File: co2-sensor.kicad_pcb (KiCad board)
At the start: 2 copper layers, 159.5 x 116 mm, 20 parts, among them J1 E-Ink Display, Q1 Si1308EDL

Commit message: Rework to use ESP32 module directly
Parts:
- removed A2: Adafruit Feather, Module:Adafruit_Feather
- added C11: 10uF, Capacitor_SMD:C_0805_2012Metric, F.Cu at (94.4, 75.0)
- added C12: 10uF, Capacitor_SMD:C_0805_2012Metric, F.Cu at (94.4, 78.0)
- added C13: 1uF, Capacitor_SMD:C_0805_2012Metric, F.Cu at (71.8, 78.5)
- added C14: 100nF, Capacitor_SMD:C_0805_2012Metric, F.Cu at (71.8, 81.5)
- added C15: 4.7uF, Capacitor_SMD:C_0805_2012Metric, F.Cu at (111.5, 106.6)
- added C16: 22uF, Capacitor_SMD:C_0805_2012Metric, F.Cu at (76.2, 75.4)
- added C17: 100nF, Capacitor_SMD:C_0805_2012Metric, F.Cu at (76.2, 78.5)
- added D4: SS14, Diode_SMD:D_SOD-123, F.Cu at (72.5, 84.6)
- added J2: USB-C Receptacle, Connector_USB:USB_C_Receptacle_G-Switch_GT-USB-7010ASV, F.Cu at (98.0, 94.0)
- added J3: JST 2-PH, Connector_JST:JST_PH_S2B-PH-SM4-TB_1x02-1MP_P2.00mm_Horizontal, F.Cu at (104.2, 110.7)
- added Q3: DMP2045U, Package_TO_SOT_SMD:SOT-23, F.Cu at (72.0, 88.7)
- added R10: 10k, Capacitor_SMD:C_0805_2012Metric, F.Cu at (103.3, 78.0)
- added R11: 10k, Capacitor_SMD:C_0805_2012Metric, F.Cu at (111.5, 109.6)
- added R12: 2k, Capacitor_SMD:C_0805_2012Metric, F.Cu at (111.5, 112.6)
- added R13: 10k, Capacitor_SMD:C_0805_2012Metric, F.Cu at (80.7, 78.5)
- added R14: 100k, Capacitor_SMD:C_0805_2012Metric, F.Cu at (80.7, 81.5)
- added R3: 5.1k, Capacitor_SMD:C_0805_2012Metric, F.Cu at (94.4, 87.1)
- added R4: 5.1k, Capacitor_SMD:C_0805_2012Metric, F.Cu at (98.8, 75.0)
- added R5: 100k, Capacitor_SMD:C_0805_2012Metric, F.Cu at (98.8, 78.0)
- added R6: 10k, Capacitor_SMD:C_0805_2012Metric, F.Cu at (76.2, 81.5)
- added R7: 5.1k, Capacitor_SMD:C_0805_2012Metric, F.Cu at (80.7, 75.4)
- added R8: 10k, Capacitor_SMD:C_0805_2012Metric, F.Cu at (98.8, 87.1)
- added R9: 10k, Capacitor_SMD:C_0805_2012Metric, F.Cu at (103.3, 75.0)
- added SW1: SW_Push, Button_Switch_SMD:SW_SPST_SKQG_WithStem, F.Cu at (64.8, 77.3)
- added SW2: SW_Push, Button_Switch_SMD:SW_SPST_SKQG_WithStem, F.Cu at (64.8, 84.1)
- added SW3: SW_Push, Button_Switch_SMD:SW_SPST_SKQG_WithStem, F.Cu at (87.4, 90.4)
- added SW4: SW_Push, Button_Switch_SMD:SW_SPST_SKQG_WithStem, F.Cu at (87.4, 97.2)
- added SW5: SW_Push, Button_Switch_SMD:SW_SPST_SKQG_WithStem, F.Cu at (87.4, 103.9)
- added SW6: SW_Push, Button_Switch_SMD:SW_SPST_SKQG_WithStem, F.Cu at (64.8, 90.8)
- added U1: ESP32-C6-MINI-1/U, PCM_Espressif:ESP32-C6-MINI-1, F.Cu at (70.3, 103.6)
- added U2: AP2112K-3.3, Package_TO_SOT_SMD:SOT-23-5, F.Cu at (103.4, 86.0)
- added U3: MCP73831T-2ACI/OT, Package_TO_SOT_SMD:SOT-23-5, F.Cu at (111.9, 116.5)
- added U4: MAX17048, Package_DFN_QFN:DFN-8-1EP_2x2mm_P0.5mm_EP1.05x1.75mm, F.Cu at (76.6, 88.2)
- J1: value E-Ink Display -> Waveshare E-Ink
- R1: value 10K -> 10k
- R2: value 3 -> 3Ω
- moved A1 108.1 mm to (80.3, 129.5)
- moved C5 40.2 mm to (71.8, 75.4), turned to 0 degrees
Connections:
- A1 pad 4: /SDA -> /I2C_SDA
- A1 pad 5: /SCL -> /I2C_SCL
- C2 pad 2: /PREVGL -> Net-(J1-Pin_22)
- C3 pad 2: Net-(J1-Pin_22) -> Net-(J1-Pin_20)
- C4 pad 2: Net-(J1-Pin_20) -> Net-(J1-Pin_18)
- C5 pad 2: Net-(J1-Pin_18) -> /PREVGL
- J1 pad 13: /SCL -> /EINK_SCLK
- J1 pad 14: /SDA -> /EINK_MOSI
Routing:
- net /SDA: track 3.35 -> 0.00 mm, vias 1 -> 0
- net /EINK_MOSI: track 0.00 -> 3.35 mm, vias 0 -> 1
- net /SCL: track 3.22 -> 0.00 mm, vias 1 -> 0
- net /EINK_SCLK: track 0.00 -> 3.22 mm, vias 0 -> 1
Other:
- board size 159.5 x 116 mm -> 92.5 x 70.5 mm

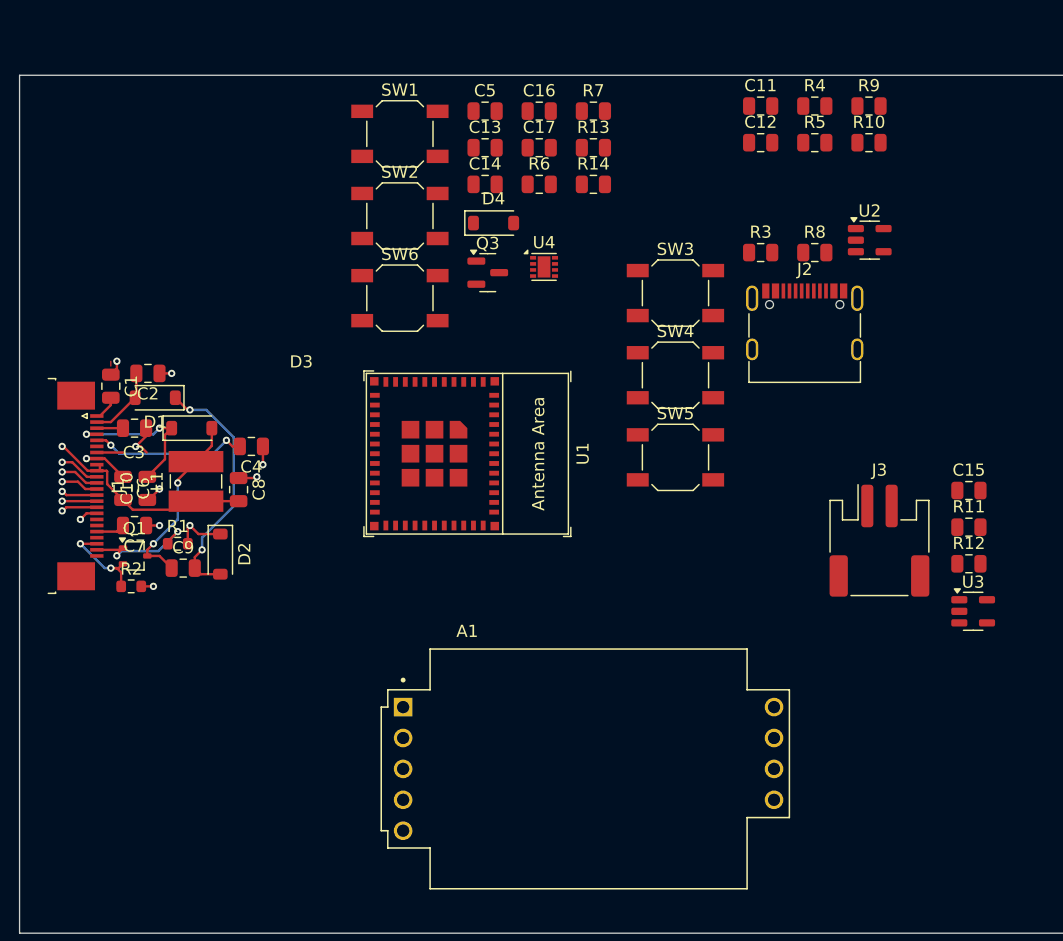
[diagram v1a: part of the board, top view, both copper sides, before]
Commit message: Update PCB from schematic
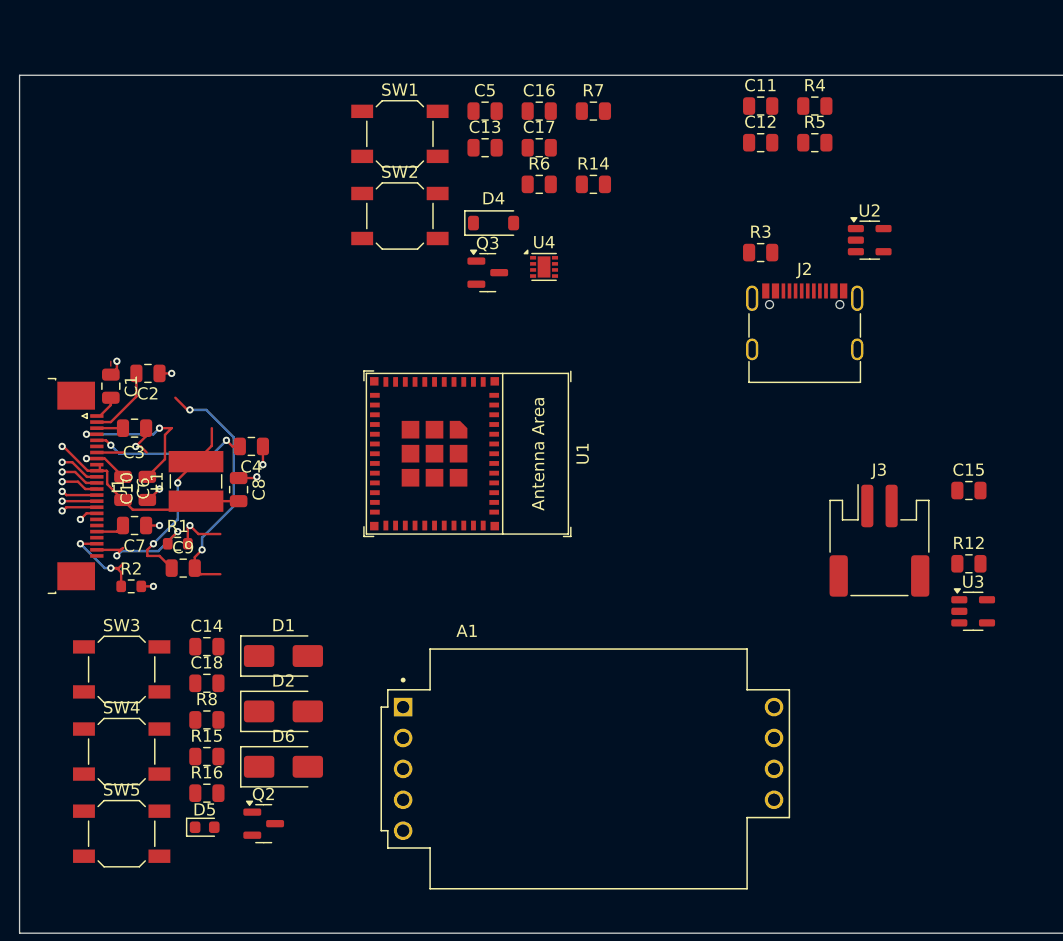
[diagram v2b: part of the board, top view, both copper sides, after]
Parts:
- removed D3: MBR0530, Diode_SMD:D_SOD-123
- removed Q1: Si1308EDL, Package_TO_SOT_SMD:SOT-323_SC-70
- removed R10, R11, R13, R9: 10k, Capacitor_SMD:C_0805_2012Metric
- removed SW6: SW_Push, Button_Switch_SMD:SW_SPST_SKQG_WithStem
- added C18: 100nF, Capacitor_SMD:C_0805_2012Metric, F.Cu at (48.9, 122.5)
- added D5: Vf=2.8V, If=1mA, LED_SMD:LED_0603_1608Metric, F.Cu at (48.7, 134.3)
- added D6: SS14, Diode_SMD:D_SMA, F.Cu at (55.2, 129.3)
- added Q2: AO3400A, Package_TO_SOT_SMD:SOT-23, F.Cu at (53.6, 134.0)
- added R15: 5.1k, Capacitor_SMD:C_0805_2012Metric, F.Cu at (48.9, 128.5)
- added R16: 5.1k, Capacitor_SMD:C_0805_2012Metric, F.Cu at (48.9, 131.5)
- C14: value 100nF -> 4.7uF
- D1, D2: value MBR0530 -> SS14; footprint Diode_SMD:D_SOD-123 -> Diode_SMD:D_SMA
- R2: value 3Ω -> 2Ω
- R7: value 5.1k -> 10k
- R8: value 10k -> 2k
- moved R8 63.0 mm to (48.9, 125.5)
- moved SW3 55.0 mm to (41.9, 121.3)
- moved SW4 55.0 mm to (41.9, 128.1)
- moved SW5 55.0 mm to (41.9, 134.8)
- moved C14 44.3 mm to (48.9, 119.5)
- moved D1 23.7 mm to (55.2, 120.2), turned to 0 degrees
- moved D2 13.9 mm to (55.2, 124.8), turned to 0 degrees
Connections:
- C14 pad 1: GND -> VBUS
- C14 pad 2: /BOOT9 -> GND
- C9 pad 1: Net-(D3-A) -> Net-(D2-A)
- C9 pad 2: Net-(D1-K) -> Net-(D1-A)
- D1 pad 1: Net-(D1-K) -> GND
- D1 pad 2: /PREVGL -> Net-(D1-A)
- D2 pad 1: GND -> /PREVGH
- D2 pad 2: Net-(D1-K) -> Net-(D2-A)
- L1 pad 2: Net-(D3-A) -> Net-(D2-A)
- R8 pad 1: /BTN1 -> Net-(U3-STAT)
- R8 pad 2: GND -> Net-(D5-K)
- SW3 pad 1: /BTN1 -> GND
- SW3 pad 2: +3.3V -> /BTN1
- SW4 pad 1: /BTN2 -> GND
- SW4 pad 2: +3.3V -> /BTN2
- SW5 pad 1: /BTN3 -> GND
- SW5 pad 2: +3.3V -> /BTN3
- U1 pad 11: Net-(U1-GND-Pad11) -> GND
- U1 pad 14: Net-(U1-GND-Pad11) -> GND
- U1 pad 19: /EINK_BUSY -> unconnected-(U1-GPIO14-Pad19)
- U1 pad 2: Net-(U1-GND-Pad11) -> GND
- U1 pad 28: /BAT_STAT -> unconnected-(U1-GPIO22-Pad28)
- U1 pad 36: Net-(U1-GND-Pad11) -> GND
- U1 pad 37: Net-(U1-GND-Pad11) -> GND
- U1 pad 38: Net-(U1-GND-Pad11) -> GND
- U1 pad 39: Net-(U1-GND-Pad11) -> GND
- U1 pad 40: Net-(U1-GND-Pad11) -> GND
- U1 pad 41: Net-(U1-GND-Pad11) -> GND
- U1 pad 42: Net-(U1-GND-Pad11) -> GND
- U1 pad 43: Net-(U1-GND-Pad11) -> GND
- U1 pad 44: Net-(U1-GND-Pad11) -> GND
- U1 pad 45: Net-(U1-GND-Pad11) -> GND
- U1 pad 46: Net-(U1-GND-Pad11) -> GND
- U1 pad 47: Net-(U1-GND-Pad11) -> GND
- U1 pad 48: Net-(U1-GND-Pad11) -> GND
- U1 pad 49: Net-(U1-GND-Pad11) -> GND
- U1 pad 50: Net-(U1-GND-Pad11) -> GND
- U1 pad 51: Net-(U1-GND-Pad11) -> GND
- U1 pad 52: Net-(U1-GND-Pad11) -> GND
- U1 pad 53: Net-(U1-GND-Pad11) -> GND
- U1 pad 6: /BTN4 -> /EINK_BUSY
- U3 pad 1: /BAT_STAT -> Net-(U3-STAT)
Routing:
- net Net-(D1-K): track 20.5 -> 0.00 mm, vias 2 -> 0
- net Net-(D1-A): track 0.00 -> 20.5 mm, vias 0 -> 2
- net Net-(D3-A): track 15.1 -> 0.00 mm, vias 2 -> 0
- net Net-(D2-A): track 0.00 -> 15.1 mm, vias 0 -> 2
